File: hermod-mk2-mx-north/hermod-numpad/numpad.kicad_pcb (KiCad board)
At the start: 2 copper layers, 92.1 x 99.3 mm, 48 parts

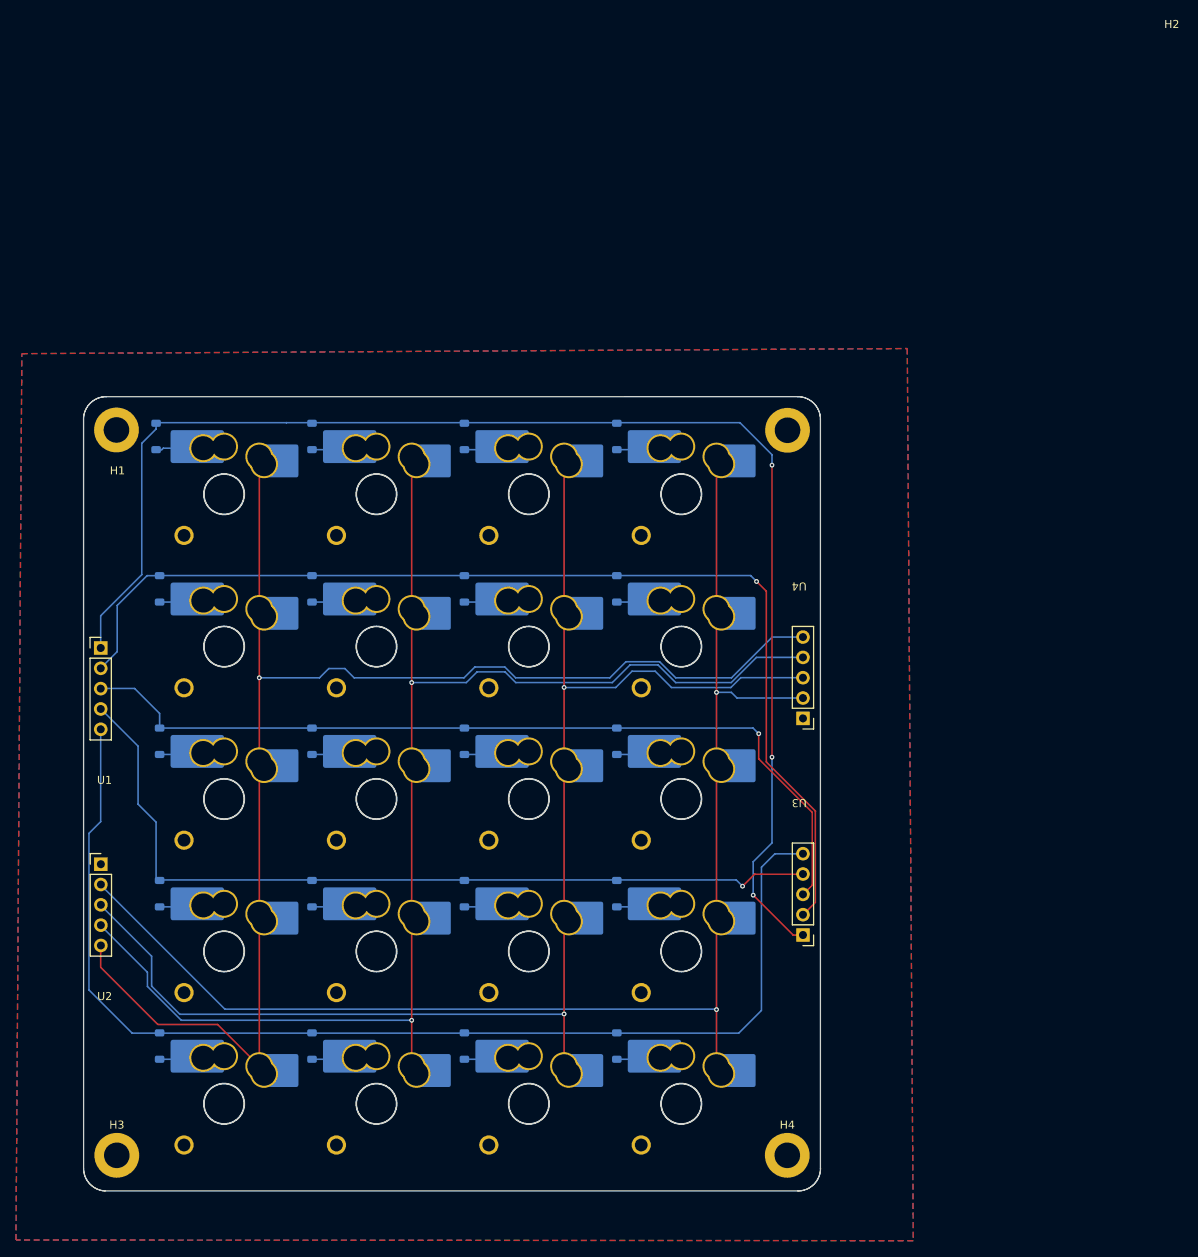
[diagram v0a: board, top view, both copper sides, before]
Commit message: Updated numpad for hermod-mk2-mk-north
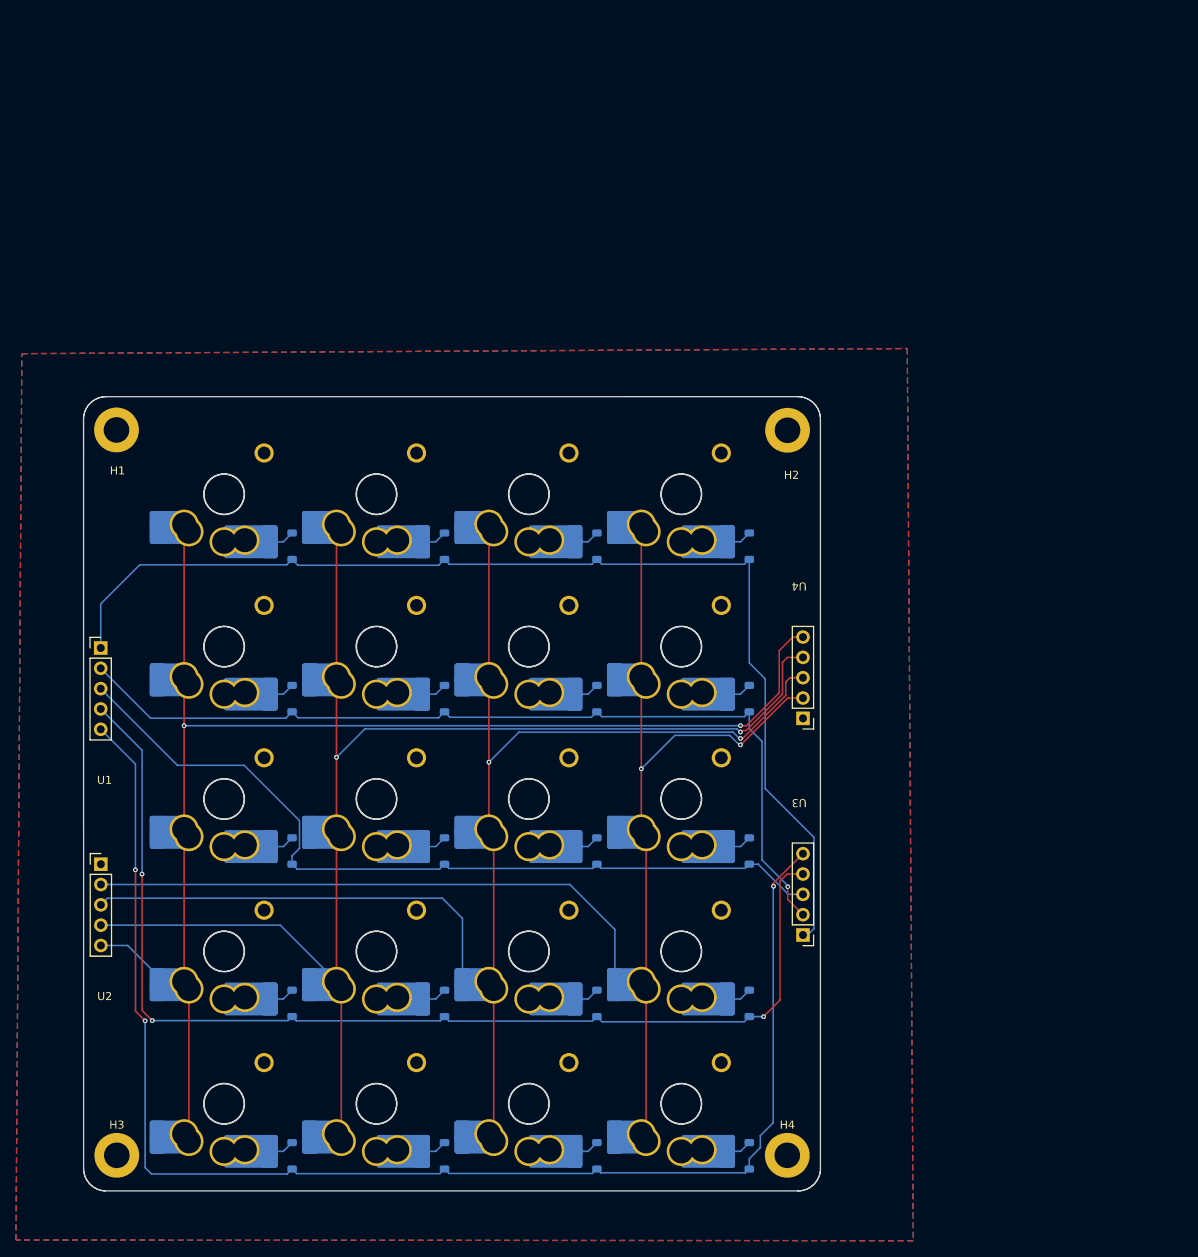
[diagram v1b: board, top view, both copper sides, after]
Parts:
- moved D1 21.8 mm to (46.6, 44.6), turned to 90 degrees
- moved D10 21.5 mm to (65.7, 82.7), turned to 90 degrees
- moved D11 21.5 mm to (84.7, 82.7), turned to 90 degrees
- moved D12 21.5 mm to (103.8, 82.7), turned to 90 degrees
- moved D13 21.5 mm to (46.6, 101.8), turned to 90 degrees
- moved D14 21.5 mm to (65.7, 101.8), turned to 90 degrees
- moved D15 21.5 mm to (84.7, 101.8), turned to 90 degrees
- moved D16 21.5 mm to (103.8, 101.8), turned to 90 degrees
- moved D17 21.5 mm to (46.6, 120.8), turned to 90 degrees
- moved D18 21.5 mm to (65.7, 120.8), turned to 90 degrees
- moved D19 21.5 mm to (84.7, 120.8), turned to 90 degrees
- moved D2 21.5 mm to (65.7, 44.6), turned to 90 degrees
- moved D20 21.5 mm to (103.8, 120.8), turned to 90 degrees
- moved D3 21.5 mm to (84.7, 44.6), turned to 90 degrees
- moved D4 21.5 mm to (103.8, 44.6), turned to 90 degrees
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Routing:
- net row3: track 106.1 -> 140.7 mm, vias 1 -> 3
- net row4: track 144.5 -> 176.8 mm, vias 0 -> 3
- net row0: track 173.9 -> 141.7 mm, vias 3 -> 0
- net row1: track 135.8 -> 113.8 mm
- net col7: track 177.6 -> 169.4 mm, vias 1 -> 2
- net row2: track 109.5 -> 104.3 mm, vias 1 -> 0
- net Net-(D1-A): track 2.74 -> 5.61 mm
- net col8: track 174.2 -> 172.0 mm
- net col10: track 170.7 -> 171.8 mm
- net col9: track 174.0 -> 174.7 mm
